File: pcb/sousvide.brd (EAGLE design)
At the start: 45.7 x 26.7 mm, 10 parts

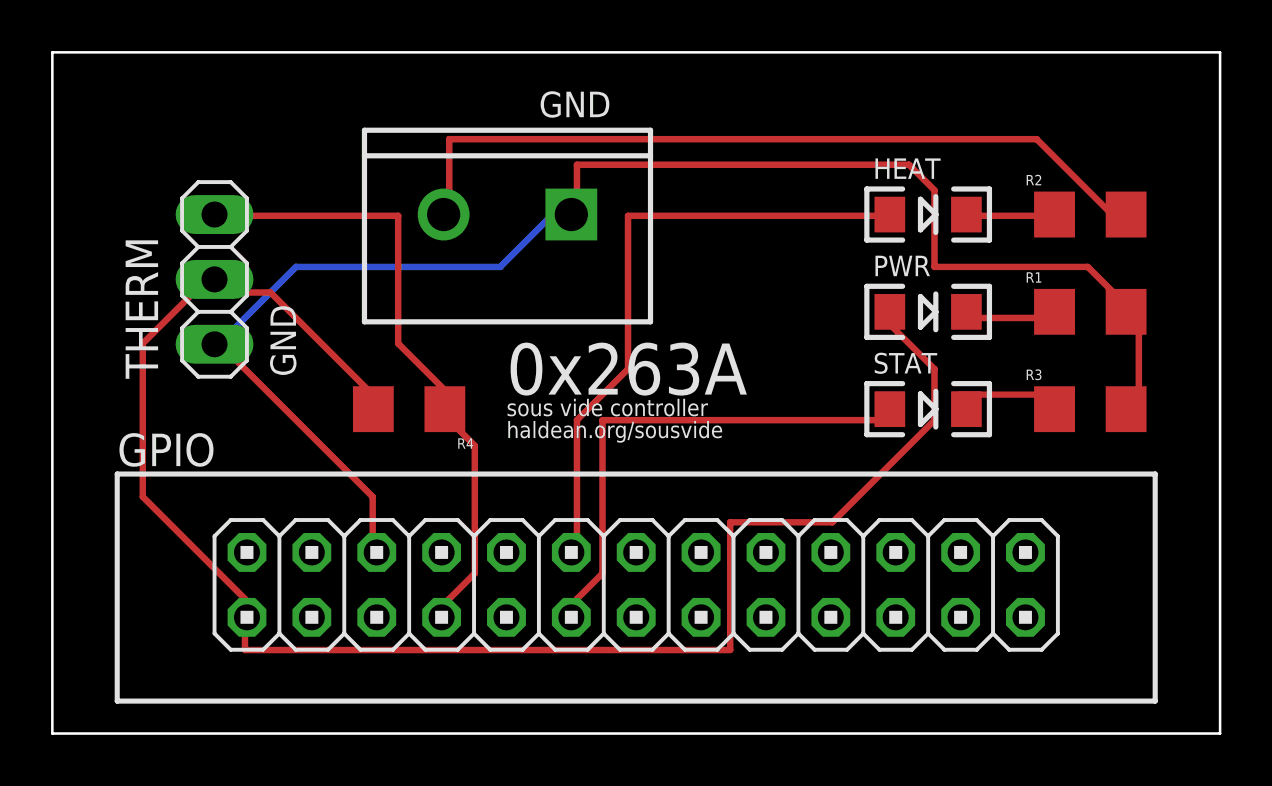
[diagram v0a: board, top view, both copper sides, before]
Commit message: Fix bug in PCB.
The first one dropped too much over the LED in line with the heater relay, so
the heater relay never flipped. This removes the LED in line with the heater and
replaces it with an LED on a separate pin.

Important lesson learned: always breadboard your designs before you fab them.
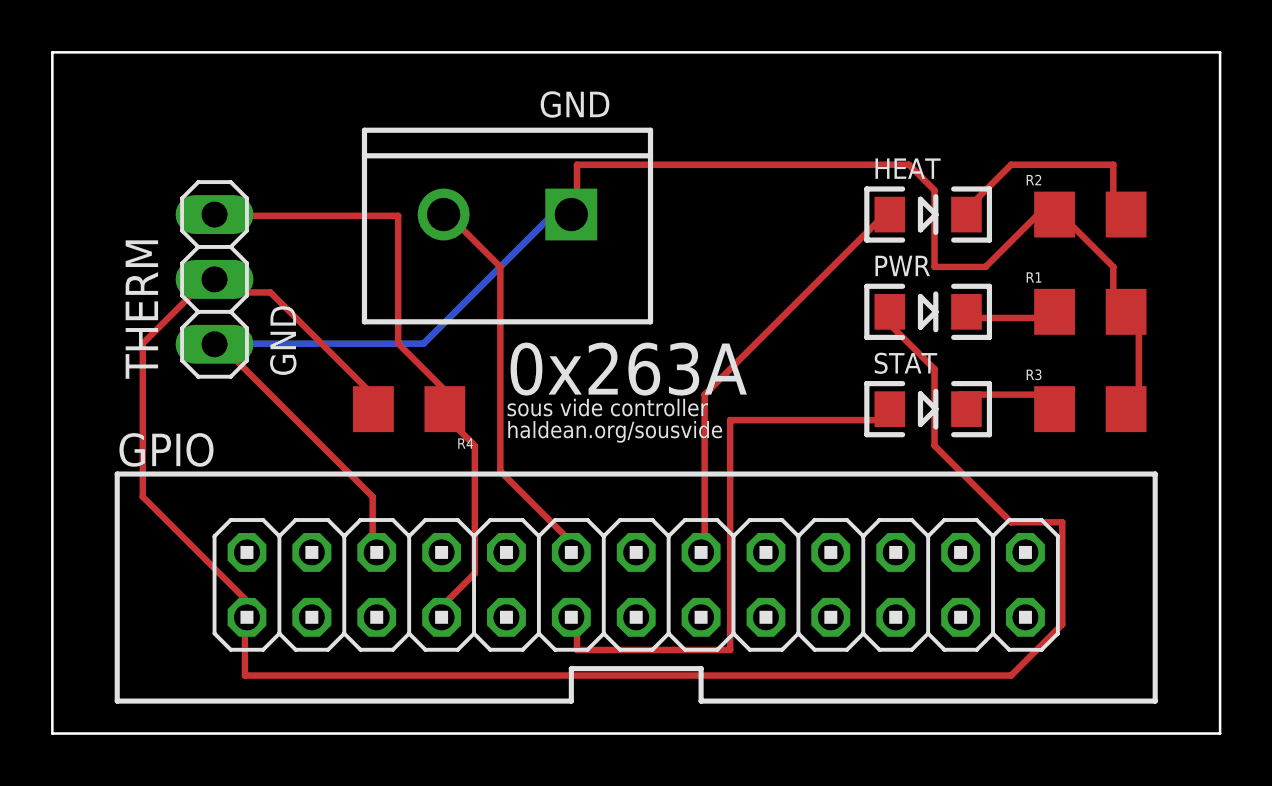
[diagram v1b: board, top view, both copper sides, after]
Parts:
- R2: device SparkFun-Passives:1206 -> SparkFun-Resistors:1206
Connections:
- net GND: now also R2.1
- net N$2: now also GPIO.12, HEATER.2; no longer HEAT.C, R2.1
- net N$4: now also GPIO.16, HEAT.A; no longer HEATER.2, R2.2
- net N$5: now also HEAT.C, R2.2; no longer GPIO.12, HEAT.A
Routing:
- net N$5: track 24.4 -> 9.59 mm
- net N$4: track 30.7 -> 16.4 mm
- net N$2: track 3.96 -> 15.6 mm
- net 3V3: track 65.1 -> 76.5 mm
- net N$6: track 19.7 -> 22.9 mm
- net GND: track 59.0 -> 61.2 mm
